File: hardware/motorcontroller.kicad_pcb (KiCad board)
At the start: 4 copper layers, 110 x 160 mm, 190 parts, among them J101 TYPE-C-31-M-12, J102 STLink_02x05, J103 STRLCK, J104 IGN, J105 THROTTLE, J106 UART, J107 IO, J108 DIR, J109 EN, J110 CAN, J201 FUSE, Q101 AP2300, Q401 STP15810, Q402 STP15810, Q403 STP15810, Q404 STP15810, Q405 STP15810, Q406 STP15810, Q407 STP15810, Q408 STP15810, Q409 STP15810, Q410 STP15810, Q411 STP15810, Q412 STP15810, Q501 WSP6946, Q502 WSP6946, SW301 SW_Push, U101 SN65HVD231DR, U201 LM2596HVGT-ADJ, U202 XL1509-3.3E1, U203 STM32F103C8Tx, U301 M95640-WMN6TP, U401 LM5110-1MX, U402 LM5110-1MX, U403 LM5110-1MX, U404 LM5110-1MX, U405 LM5110-1MX, U406 LM5110-1MX, Y301 8MHz

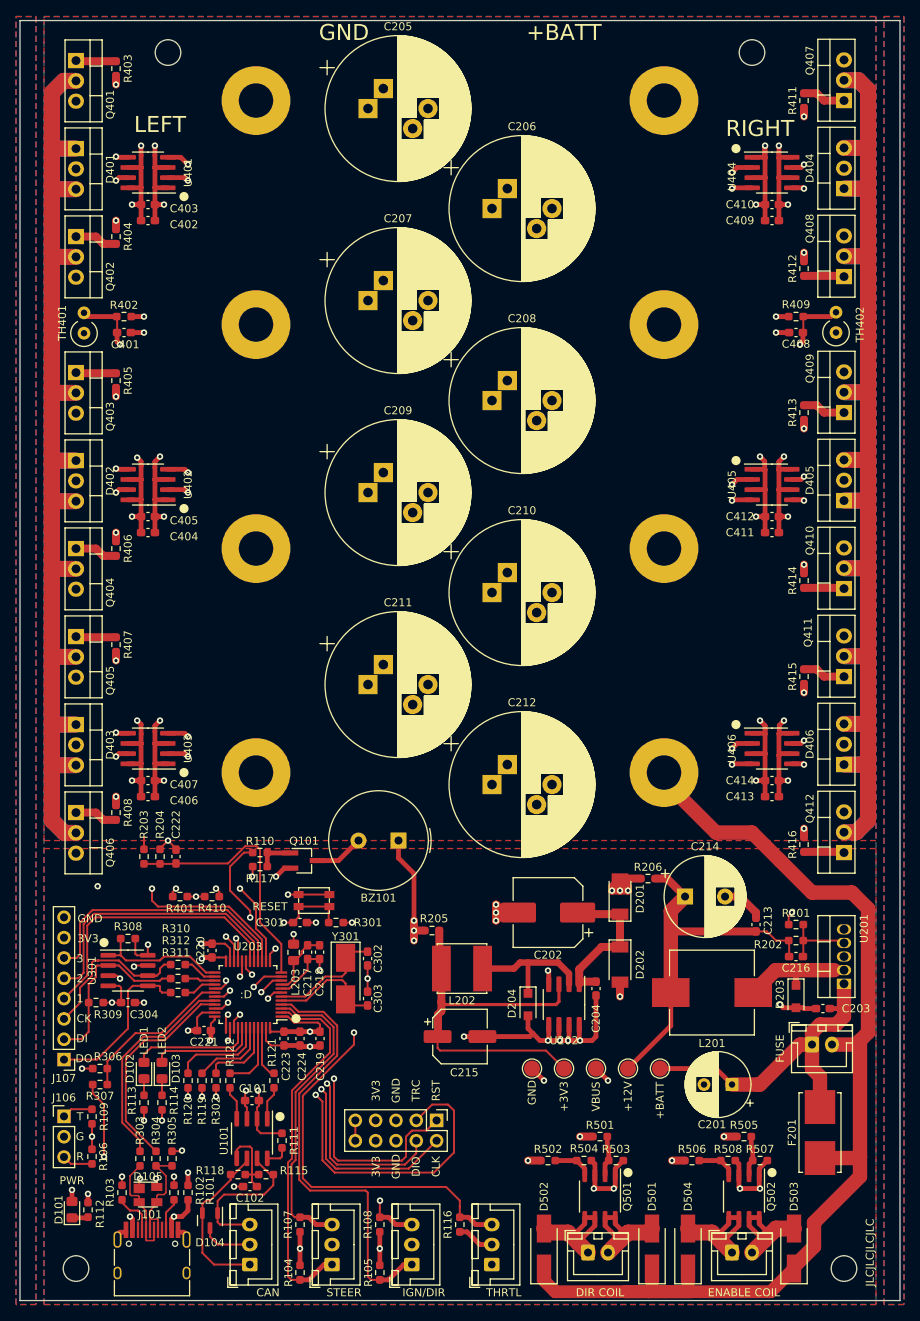
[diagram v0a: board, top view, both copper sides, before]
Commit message: Change diode package to isolated TO220
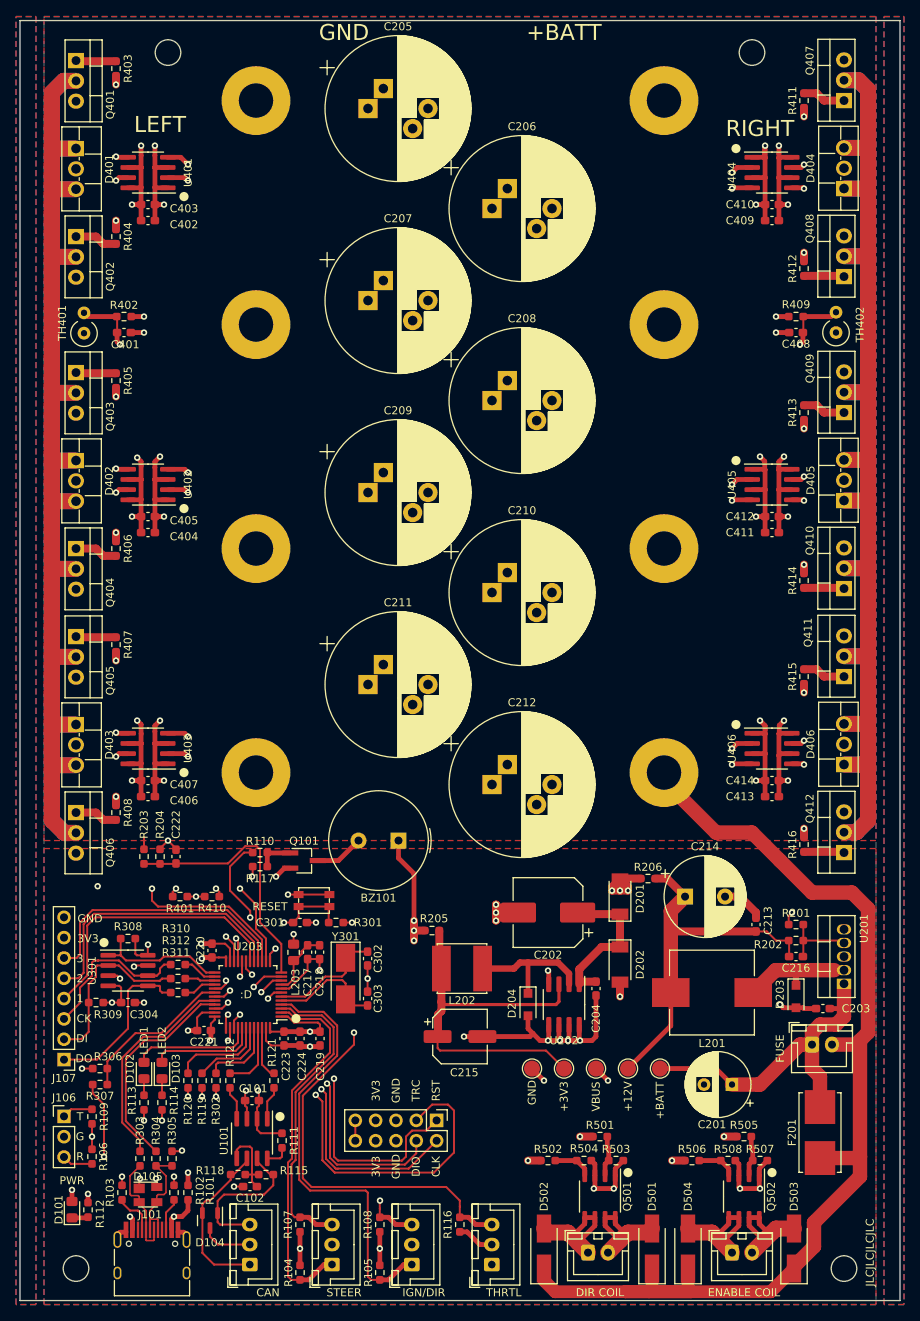
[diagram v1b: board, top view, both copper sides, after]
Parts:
- D401, D402, D403, D404, D405, D406: footprint Package_TO_SOT_THT:TO-220-3_Vertical -> Package_TO_SOT_THT:TO-220F-3_Vertical
